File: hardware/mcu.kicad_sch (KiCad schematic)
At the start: 28 parts, among them SW1 BOOT / PTS810, SW2 RESET / PTS810, U2 ESP32-C6-WROOM-1, U4 BQ32000, Y1 32.768kHz

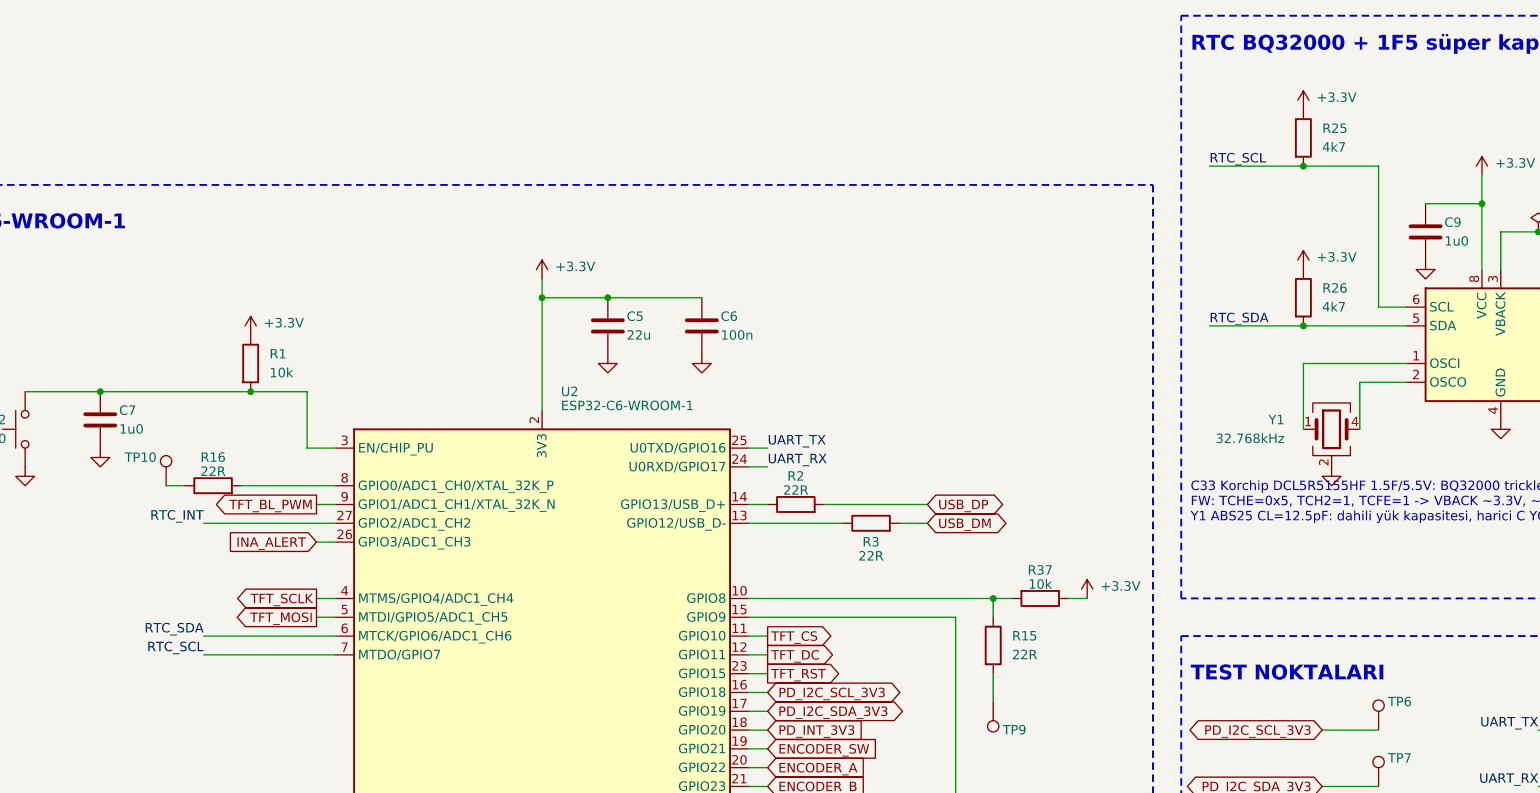
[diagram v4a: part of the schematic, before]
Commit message: hardware: çıkış anahtarını LM74801'e geçir, USB-C korumasını ve OUT_EN'i düzelt
Çıkış anahtarı / ters akım (usb_pd_controller):
- U12 AP74502Q -> LM74801-Q1 (LM74801QDRRRQ1, WSON-12, EP boşta). AP74502Q
  ideal diyot değil; çıkış açıkken ters akım doğrudan adaptör VBUS'ına
  gidiyordu. Ortak-source Q5: HGATE -> Q5A (GATE_DRV, R54/C30, D6),
  DGATE -> Q5B (yeni net), A/OUT = SRC_COMMON, C = SW_OUT, VS/VSNS/SW = V_PRE.
- R55 232k -> 237k: LM74801 OV 30.4 V (29.5-31.3 V), 28 V EPR +%5 üstünde.
- OUT_EN kapatamıyordu (EN ~1.57 V > 1.32 V): R57 kalktı, U13 74LVC1G08
  (SN74LVC1G08DBVR) EN = OUT_EN AND ~ALERT; R61 4k7 OUT_EN pull-down, C35.
- AOZ1284 kompanzasyonu: R41 12k7 -> 51k, C19 18n -> 15n (fC ~5 -> ~20 kHz).
- Q3/Q5 footprint: yeni Package_SO_Custom:Vishay_PowerPAK_SO-8L_Dual
  (Vishay doc 63817'den ölçüldü; 6/8 yalnız bakır eş drain pedleri).
- TL431DBZ önbelleği KiCad 10 kütüphanesinden yenilendi (pin uçları aynı).

MCU:
- RTC (BQ32000) PD/INA226 I2C bus'ına alındı, R25/R26 kalktı; OUT_EN = GPIO6
  (MTCK), GPIO7 boş.

USB-C girişi (usb_c_input):
- CC1/CC2'ye Rd 5k1 (R62/R63) eklendi; AP33772S Figure 1 harici Rd istiyor,
  şemada hiç yoktu.
- CC1/CC2 5.5 V'luk U10'dan ayrıldı (AP33772S CC 34 V'a dayanır, U10 28 V
  kısa devrede yanardı); D8/D9 SMF30A CC ESD opsiyonu DNP.
- U10 TPD4EUSB30 -> USBLC6-2SC6 (yalnız D+/D-, jumper_pin_groups ile
  flow-through, VBUS pini +3.3V). D3 SMBJ30A yer için sağa taşındı.

Doğrulama: her adımda beklenen netlist farkı; son durum ERC 0 hata / 0 uyarı,
101 net. Parçalar Özdisan stoğundan (SelectionNote alanlarında).

Kayıtlar:
- todo.txt açık kalanlara göre yeniden düzenlendi.
- design_decisions/output/SEMA_TAMAMLANAN_TODO_REV_C_20260922.md: bu
  maddelerin gerekçe ve hesapları.
- design_decisions/output/CIKIS_GERILIMI_28V_TAVANI_20260922.md: 28 V tavanı.
- Datasheet'ler: LM7480-Q1, SMF (Thinking), USBLC6-2.

Co-Authored-By: Claude Opus 5 <noreply@anthropic.com>
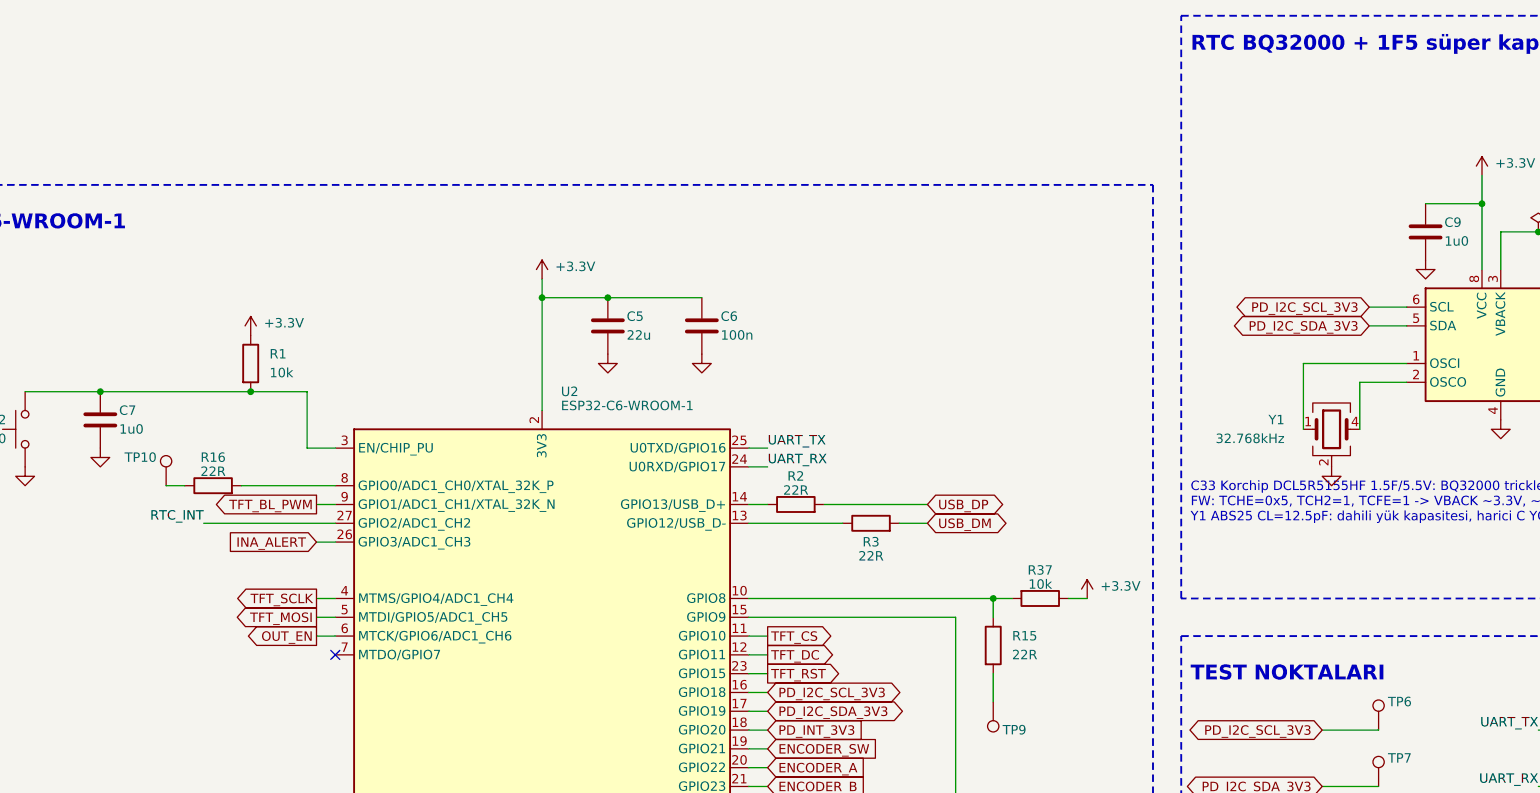
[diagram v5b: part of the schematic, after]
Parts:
- removed R25, R26: 4k7, Resistor_SMD:R_0402_1005Metric, symbol Device:R
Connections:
- net PD_I2C_SCL_3V3: now also U4.6 (SCL)
- net PD_I2C_SDA_3V3: now also U4.5 (SDA)
- net RTC_SCL: no longer names the net of U2.7 (MTDO/GPIO7)
- net RTC_SCL: no longer U4.6 (SCL)
- net RTC_SDA renamed OUT_EN
- net OUT_EN: no longer U4.5 (SDA)
- no-connect marks 0 -> 1

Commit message: hardware: L1'i FPI0705-220K'ya geçir, U1/U2 tedarikini karara bağla (TASK-002)
L1 (AOZ1284 buck bobini): SRI0704-220M Özdisan'da stokta yok.
"Sabit İndüktörler" kategorisinde 22 µH taraması datasheet'lerle
karşılaştırıldı; FPI0705-220K seçildi (Özdisan 507505, stok 3467, 8,28 TL):
- 22 µH ±10%, RDC 0,11 Ω max (tasarımdakiyle aynı), IDC 1,95 -> 2,3 A.
- Gövde 7,3x7,3x4,5 -> 7,8x7,0x5,0 mm; yeni footprint
  Inductor_Custom:L_CoreMaster_FPI0705_7.8x7.0mm_H5.0 (land 7,5x3,25 mm
  iki ped, 2,0 mm boşluk; spec DWG MY0212071), fp-lib-table'a eklendi.
- Reddedilenler: TPY0705-220M (mevcut footprint'e uyuyor ama 0,35 Ω),
  SRI0704-330M (aynı ayak, 0,25 Ω / 1,2 A), FPI1005-220M (0,07 Ω / 3,4 A,
  10x9 mm), IHLP2525CZER220M11 (62 TL).

U1 AP33772S ve U2 ESP32-C6-WROOM-1: Özdisan'da yok, karşılayan muadil de
yok (ESP32-C3-MINI-1-N4 GPIO sayısı yetmiyor; ESP32-WROOM-32E-N4 native
USB yok). Mouser/DigiKey katalogundan alınacak.

Kararlar SelectionNote alanlarına işlendi. Doğrulama: ERC 0 hata / 0 uyarı,
netlist farkı YOK, field_geometry farkı boş.

Ayrıntı: design_decisions/output/PARCA_TEDARIK_KARARLARI_20260922.md
Kayıt: CHANGES.TXT REV_C. TASK-002 Done.

Ayrıca kicad-schematic SKILL.md: alan görünürlüğü assert örneğindeki
O(n^2) tuzağı düzeltildi (field_visibility döngü içinde çağrılıyordu;
gerçek betikte 3+ dakika sürüyordu).

Co-Authored-By: Claude Opus 5 <noreply@anthropic.com>
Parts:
- U2: SelectionNote Özdisan (21.09.2026): Stokta yok. 21.09 üçüncü tur: ESP32-C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 -> Özdisan (21.09.2026): stokta yok; 22.09.2026 WiFi modulleri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
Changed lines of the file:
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@@
 			)
 		)
-		(property "SelectionNote" "Özdisan (21.09.2026): Stokta yok. 21.09 üçüncü tur: ESP32-C6 modülü Özdisan'da yok; özellikleri karşılayan muadil de yok. Tasarım native USB (GPIO12/13) ve ~22 GPIO kullanıyor. Stoktaki ESP32-C3-MINI-1-N4 (445 stok) native USB'ye sahip ama GPIO sayısı yetmez ve 802.15.4/Wi-Fi 6 yok. ESP32-WROOM-32E-N4 (466 stok) aynı 18x25,5 mm gövdede ama pin dizilişi farklı ve native USB yok (USB-UART köprüsü gerekir). İkisi de şema/footprint/firmware değişikliği ister."
+		(property "SelectionNote" "Özdisan (21.09.2026): stokta yok; 22.09.2026 WiFi modulleri kategorisinde ESP32-C6 yok. Stoktaki ESP32-C3-MINI-1-N4 (GPIO sayisi yetmez) ve ESP32-WROOM-32E-N4 (native USB yok) uymuyor. Karar: Mouser/DigiKey katalogundan alinacak (modul varyanti/flash satin alma oncesi sabitlenecek)."
 			(at 115.57 114.3 0)
 			(hide yes)

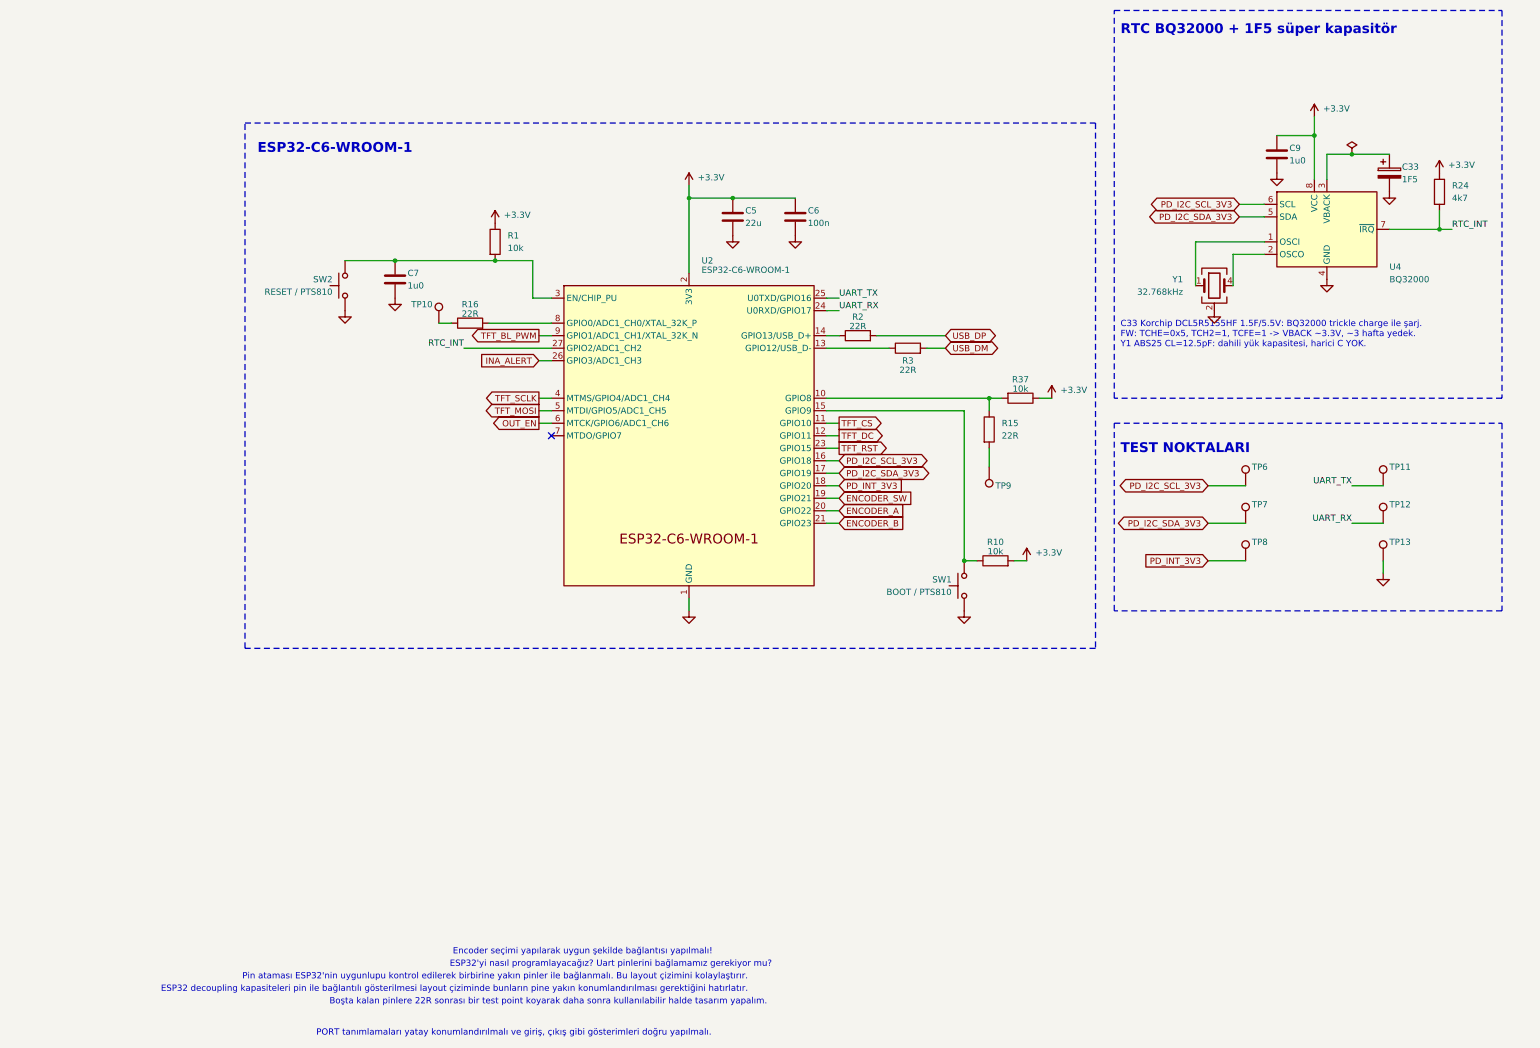
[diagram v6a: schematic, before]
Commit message: hardware: U2'yi ESP32-C6-MINI-1-H4'e geçir, şema notlarını güncelle (TASK-041/004/005)
TASK-041 — U2 ESP32-C6-WROOM-1 -> ESP32-C6-MINI-1-H4 (4 MB flash, -40..105 C,
13,2x16,6 mm). Modül IO10/IO11'i dışarı vermiyor (datasheet v1.5 Tablo 3-1):
- TFT_CS GPIO10 -> GPIO14 (pin 19), TFT_DC GPIO11 -> GPIO7 (pin 16).
- Kullanılan GPIO 0-9 ve 12-23; modülün verdiği kümeyle birebir örtüşüyor,
  boşta GPIO kalmadı. Strapping (4/5/8/9/15) rolleri değişmedi.
- Sembol/footprint KiCad standart kütüphanesinden: RF_Module:ESP32-C6-MINI-1.
- IO8/IO9 MINI-1'de sol kenarda: R37/R15/TP9 ve R10/SW1 U2'nin soluna taşındı,
  iki pull-up tek +3.3V rayını paylaşıyor (#PWR023 kalktı).
- USB seri dirençleri yerinde kaldı, taşıdıkları sinyal yer değiştirdi
  (R2 -> D-, R3 -> D+; USB_DM/USB_DP etiketleri satır değiştirdi).
- Netlist: her net U2 dışındaki üyelerini korudu (yalnız pin numaraları
  değişti), GND'ye modülün tüm toprak pedleri katıldı.

TASK-004 — Eskiyen şema notları: AOZ1284 bloğunda COMP değerleri (Rc=51k,
Cc=15n -> fC ~20 kHz), seçilen L1/D2/Cout parçaları ve "Cout: 10V X7R" hatası
düzeltildi; blok başlığı "V_PRE 5..28V INPUT" oldu. mcu sayfasında çerçeve
dışında kalmış altı eski inceleme sorusu kaldırıldı. Diğer sayfalar tarandı,
güncel.

TASK-005 — USER_İNTERFACE.kicad_sch kaldırıldı (dosya + sayfa sembolü +
.kicad_pro kaydı). İçindeki arayüz sinyal listesi docs/arayuz-sinyalleri.md'ye
güncel pin atamalarıyla taşındı. Sayfa sayısı 6 -> 5.

Doğrulama: ERC 0 hata / 0 uyarı; not/sayfa değişikliklerinde netlist farkı YOK;
okunabilirlik denetiminde yeni bulgu yok (kalan 3 bulgu eskiden beri var).

Ayrıca: TASK-006 footprint listesi güncellendi, TASK-042 açıldı (PCB
güncellemesinden sonra kullanılmayan PCM_Espressif kütüphanesini kaldır),
software/FIRMWARE_GEREKSINIMLERI.md pin haritası yenilendi.

Co-Authored-By: Claude Opus 5 <noreply@anthropic.com>
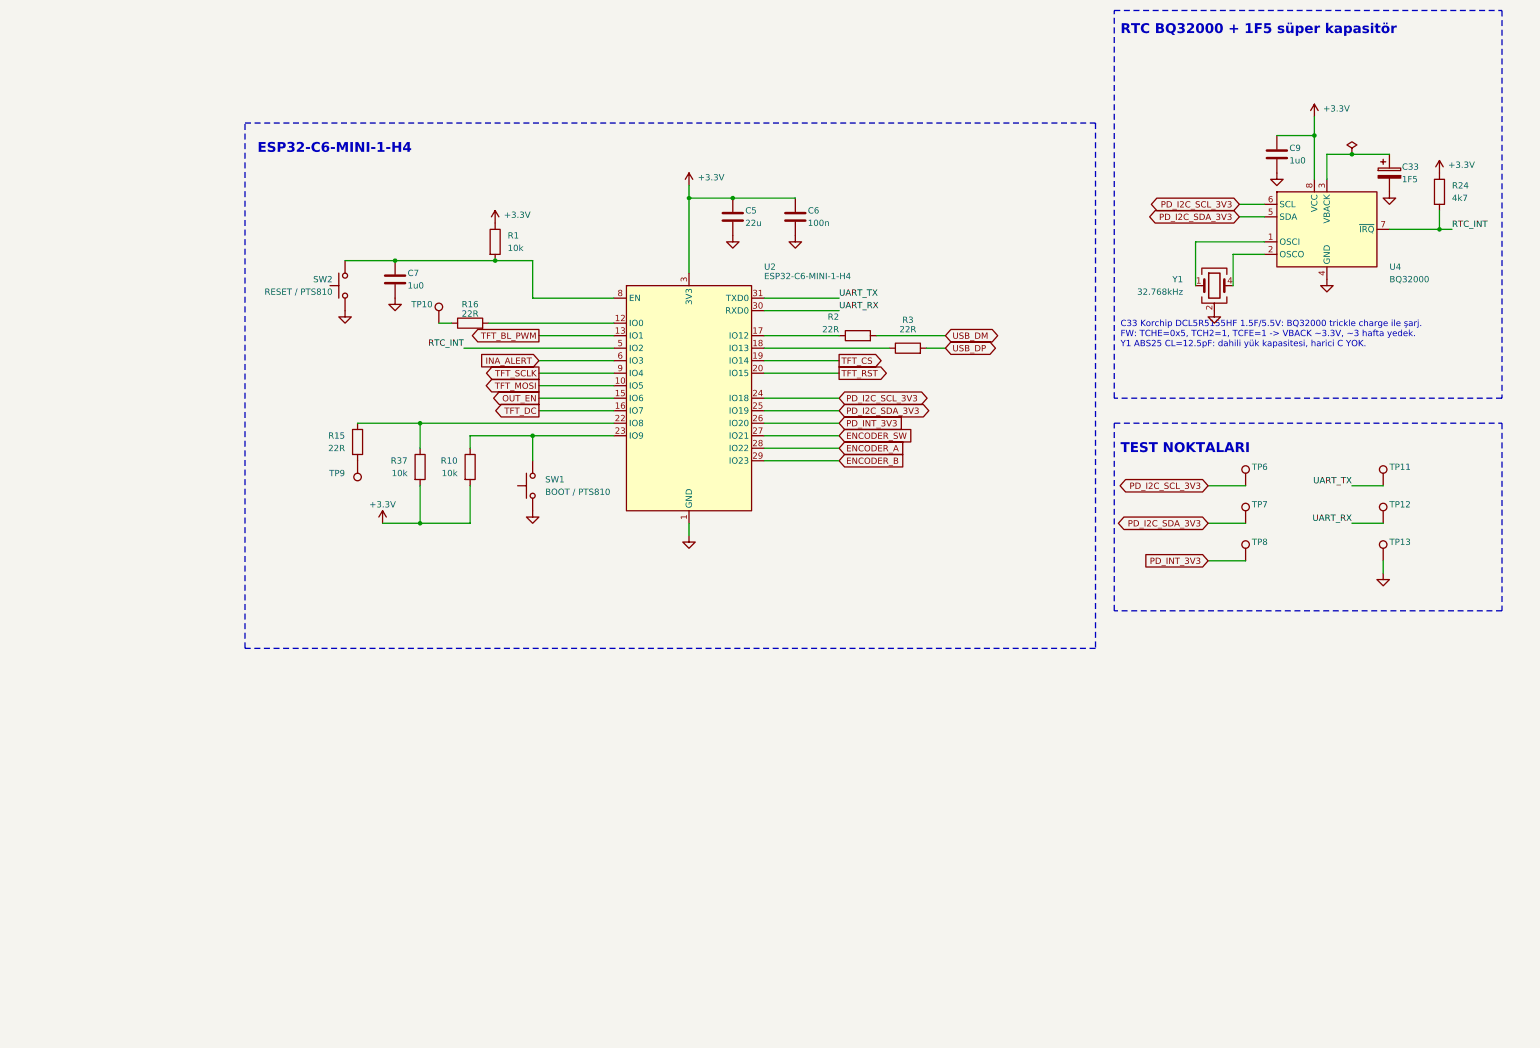
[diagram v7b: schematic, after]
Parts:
- U2: value ESP32-C6-WROOM-1 -> ESP32-C6-MINI-1-H4; footprint PCM_Espressif:ESP32-C6-WROOM-1 -> RF_Module:ESP32-C6-MINI-1; symbol PCM_Espressif:ESP32-C6-WROOM-1 -> RF_Module:ESP32-C6-MINI-1; DesignNote Modul varyanti / flash kapasitesi satin alma oncesi sabitle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 -> MINI-1 IO10/IO11 vermiyor: TFT_DC -> IO7 (pin 16), TFT_CS -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; MPN ESP32-C6-WROOM-1 -> ESP32-C6-MINI-1-H4; Package WROOM-1 Module (18x25.5mm) -> MINI-1 Module (13.2x16.6mm); SelectionNote Özdisan (21.09.2026): stokta yok; 22.09.2026 WiFi modulleri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 -> Modul varyanti 23.09.2026 kesinlesti: ESP32-C6-MINI-1-H4 (4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
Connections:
- net +3.3V: now also R37.2, U2.3 (3V3); no longer R37.1, U2.2 (3V3)
- net ENCODER_A: now also U2.28 (IO22); no longer U2.20 (GPIO22)
- net ENCODER_B: now also U2.29 (IO23); no longer U2.21 (GPIO23)
- net ENCODER_SW: now also U2.27 (IO21); no longer U2.19 (GPIO21)
- net GND: now also U2.11 (GND), U2.14 (GND), U2.2 (GND), U2.36 (GND), U2.37 (GND), U2.38 (GND), U2.39 (GND), U2.40 (GND), U2.41 (GND), U2.42 (GND), U2.43 (GND), U2.44 (GND), U2.45 (GND), U2.46 (GND), U2.47 (GND), U2.48 (GND), U2.49 (GND), U2.50 (GND), U2.51 (GND), U2.52 (GND), U2.53 (GND); no longer U2.28 (GND), U2.29 (GND)
- net INA_ALERT: now also U2.6 (IO3); no longer U2.26 (GPIO3/ADC1_CH3)
- net OUT_EN: now also U2.15 (IO6); no longer U2.6 (MTCK/GPIO6/ADC1_CH6)
- net PD_I2C_SCL_3V3: now also U2.24 (IO18); no longer U2.16 (GPIO18)
- net PD_I2C_SDA_3V3: now also U2.25 (IO19); no longer U2.17 (GPIO19)
- net PD_INT_3V3: now also U2.26 (IO20); no longer U2.18 (GPIO20)
- net RTC_INT: now also U2.5 (IO2); no longer U2.27 (GPIO2/ADC1_CH2)
- net TFT_BL_PWM: now also U2.13 (IO1); no longer U2.9 (GPIO1/ADC1_CH1/XTAL_32K_N)
- net TFT_CS: now also U2.19 (IO14); no longer U2.11 (GPIO10)
- net TFT_DC: now also U2.16 (IO7); no longer U2.12 (GPIO11)
- net TFT_MOSI: now also U2.10 (IO5); no longer U2.5 (MTDI/GPIO5/ADC1_CH5)
- net TFT_RST: now also U2.20 (IO15); no longer U2.23 (GPIO15)
- net TFT_SCLK: now also U2.9 (IO4); no longer U2.4 (MTMS/GPIO4/ADC1_CH4)
- net UART_RX: now also U2.30 (RXD0); no longer U2.24 (U0RXD/GPIO17)
- net UART_TX: now also U2.31 (TXD0); no longer U2.25 (U0TXD/GPIO16)
- net USB_DM: now also R2.2; no longer R3.2
- net USB_DP: now also R3.2; no longer R2.2
- net at R10.1, SW1.2: now also U2.23 (IO9); no longer U2.15 (GPIO9)
- net at C7.2, R1.2, SW2.2: now also U2.8 (EN); no longer U2.3 (EN/CHIP_PU)
- net at R2.1: now also U2.17 (IO12); no longer U2.14 (GPIO13/USB_D+)
- net at R3.1: now also U2.18 (IO13); no longer U2.13 (GPIO12/USB_D-)
- net at U2.22 (IO8): now also R15.1, R37.1
- net at R16.2: now also U2.12 (IO0); no longer U2.8 (GPIO0/ADC1_CH0/XTAL_32K_P)
- no-connect marks 1 -> 0
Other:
- note added: "ESP32-C6-MINI-1-H4"
- note removed: "Boşta kalan pinlere 22R sonrası bir test point koyarak daha sonra kullanılabilir halde tasarım yapalım."
- note removed: "ESP32 decoupling kapasiteleri pin ile bağlantılı gösterilmesi layout çiziminde bunların pine yakın konumlandırılması gerektiğini hatırlatır."
- note removed: "ESP32'yi nasıl programlayacağız? Uart pinlerini bağlamamız gerekiyor mu?"
- note removed: "ESP32-C6-WROOM-1"
- note removed: "Encoder seçimi yapılarak uygun şekilde bağlantısı yapılmalı!"
- note removed: "PORT tanımlamaları yatay konumlandırılmalı ve giriş, çıkış gibi gösterimleri doğru yapılmalı."
- note removed: "Pin ataması ESP32'nin uygunlupu kontrol edilerek birbirine yakın pinler ile bağlanmalı. Bu layout çizimini kolaylaştırır."
- moved on the sheet: R10, R15, R37, SW1, TP9
